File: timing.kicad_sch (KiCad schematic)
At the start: 13 parts, among them U11 CD74HC4040, U12 74LS20, U13 74LS20, U14 74LS30, U15 74LS30, U16 74LS00, U17 CD74HC4040, U18 74LS30, U19 74LS30, U20 74LS00, U3 74LS00, Y1 TFT660

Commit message: improve rom use
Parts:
- added Y2: TFT660, Oscillator:Oscillator_DIP-14, symbol Oscillator:GTXO-14T
- U12, U13: value 74LS20 -> 74HCT20
- U16, U20, U3: value 74LS00 -> 74HCT00
- Y1: Frequency (none) -> 20MHz
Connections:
- net +5V: now also Y2.1 (EN), Y2.14 (Vcc)
- net GND: now also Y2.7 (GND)
- net at JP2.1 (A), Y1.5 (OUT): now also Y2.8 (OUT)
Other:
- note added: "Clock should be 20MHz"

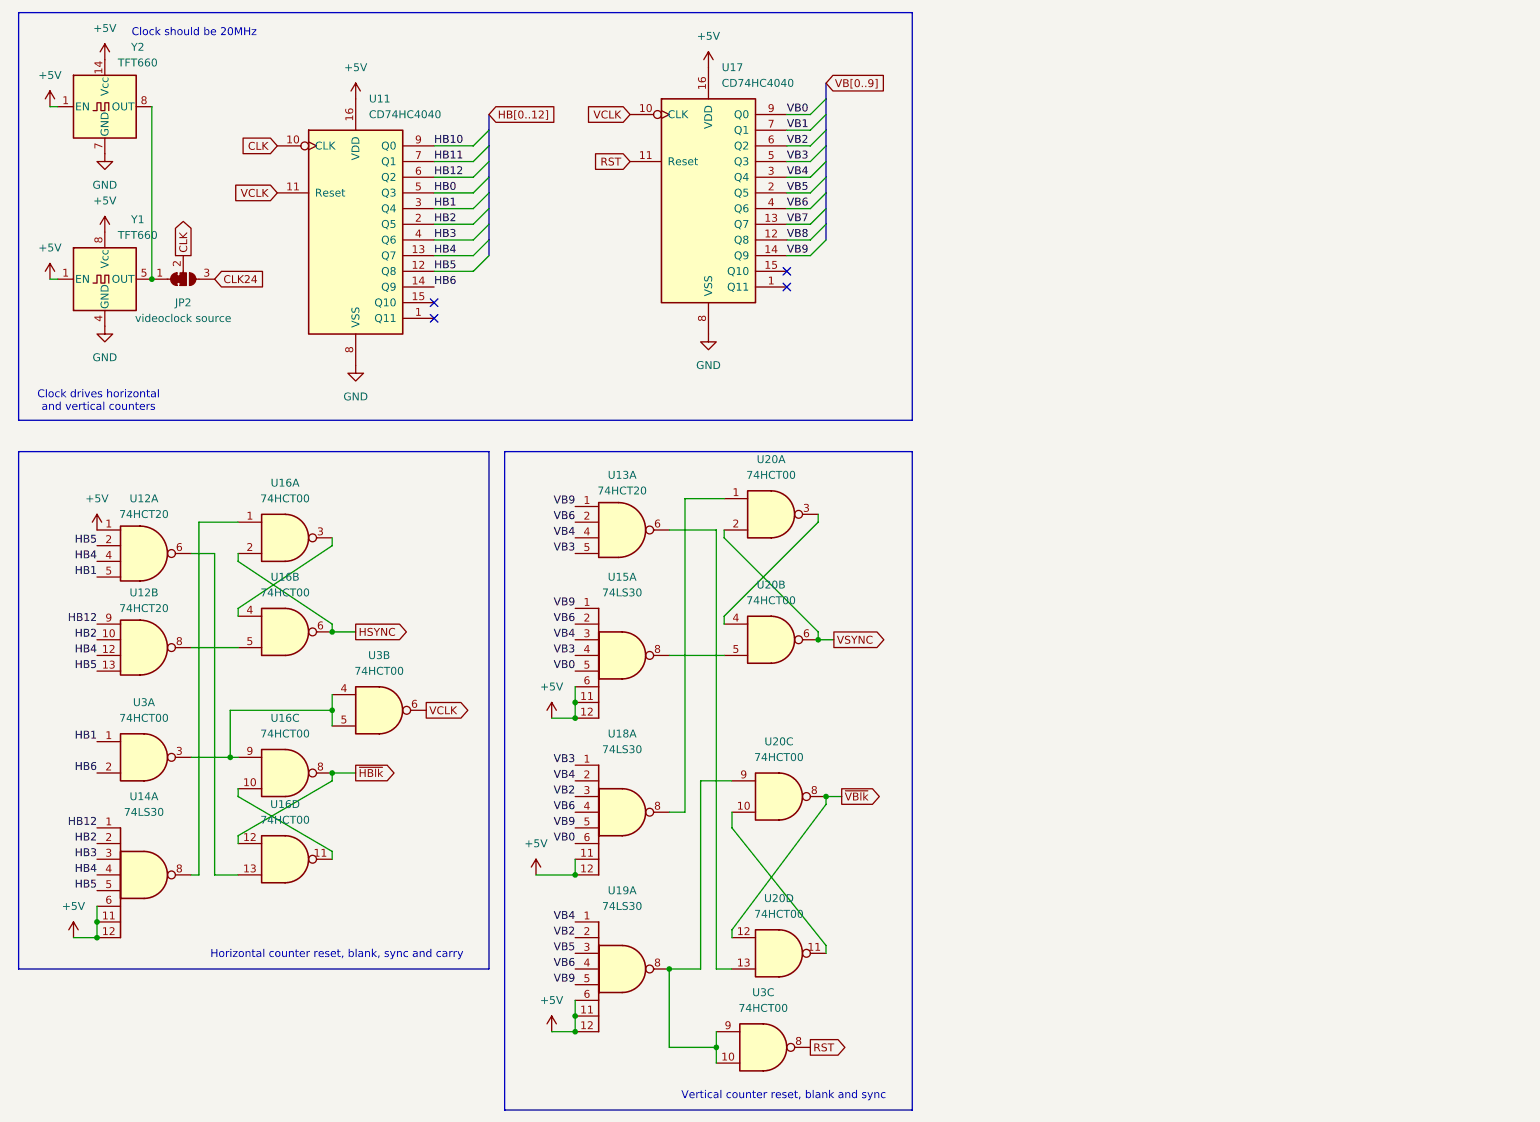
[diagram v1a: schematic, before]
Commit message: fix sync signals
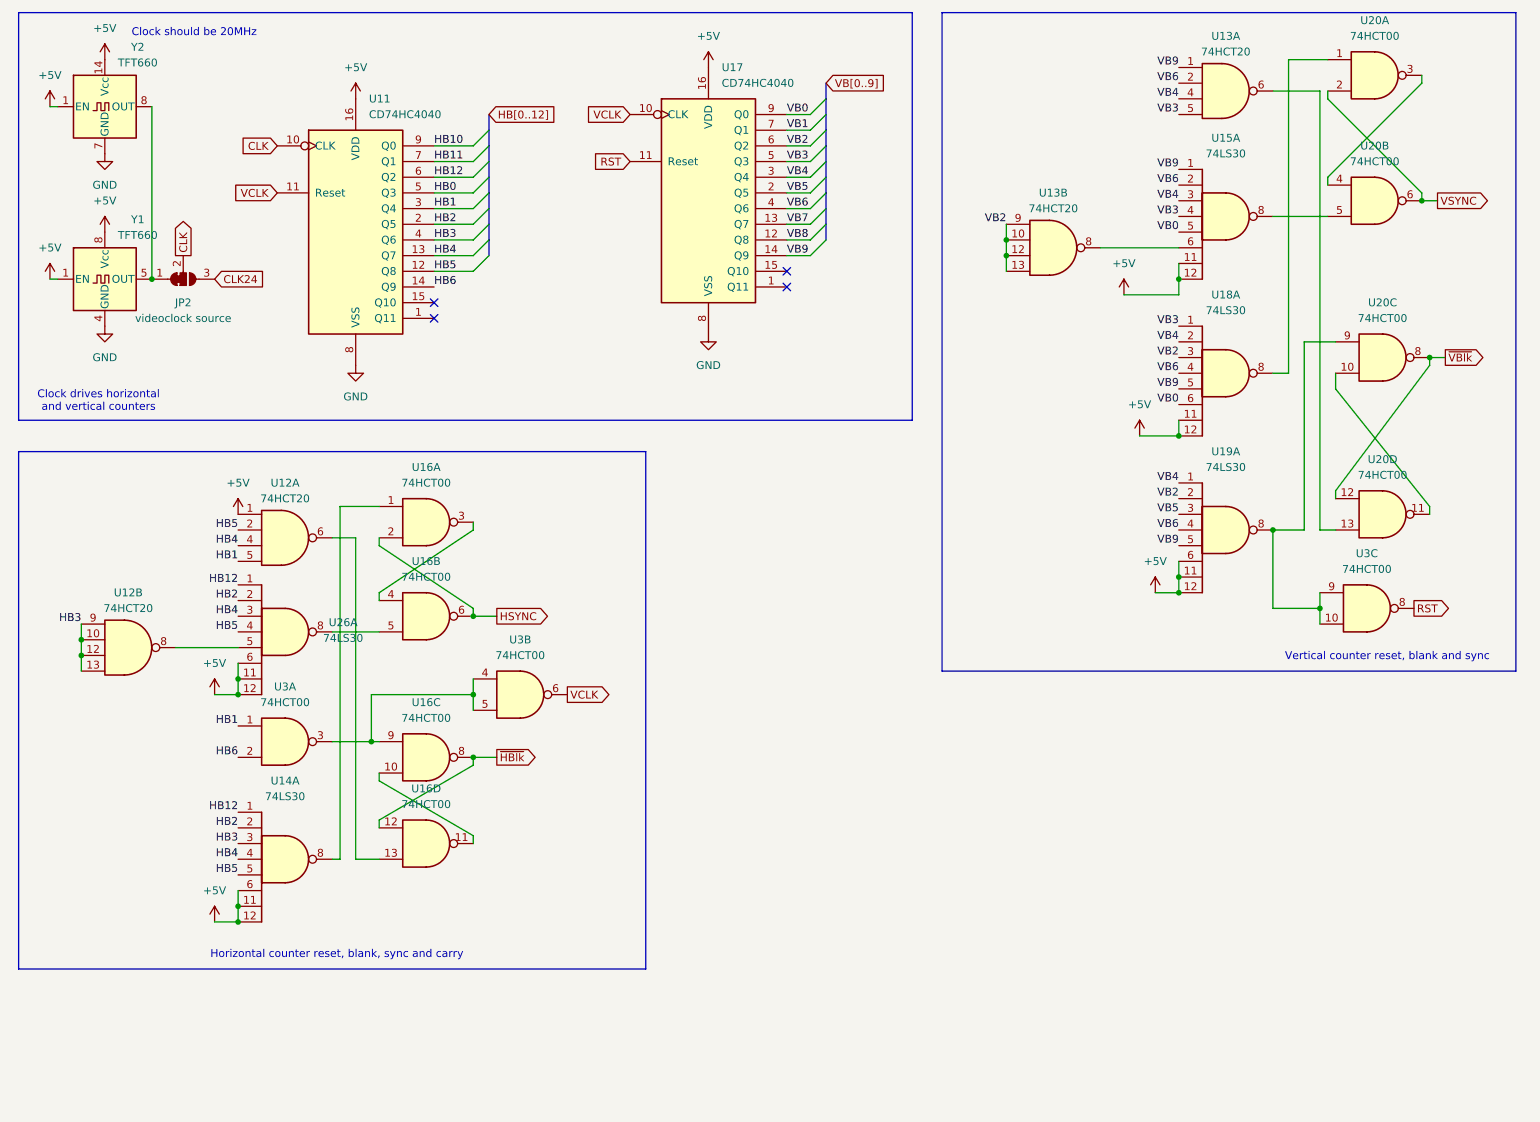
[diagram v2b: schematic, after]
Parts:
- added unit 2 of U13
- added U26: 74LS30, Package_SO:SOIC-14_3.9x8.7mm_P1.27mm, symbol 74xx:74LS30
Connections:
- net +5V: now also U26.11, U26.12, U26.6; no longer U15.6
- net HB12: now also U26.1; no longer U12.9
- net HB2: now also U26.2; no longer U12.10
- net HB3: now also U12.10, U12.12, U12.13, U12.9
- net HB4: now also U26.3; no longer U12.12
- net HB5: now also U26.4; no longer U12.13
- net VB2: now also U13.10, U13.12, U13.13, U13.9
- net at U12.8: now also U26.5; no longer U16.5
- new net: U16.5, U26.8
- new net: U13.8, U15.6
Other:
- moved on the sheet: U12A, U12B, U13A, U14A, U15A, U16A, U16B, U16C, U16D, U18A, U19A, U20A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
